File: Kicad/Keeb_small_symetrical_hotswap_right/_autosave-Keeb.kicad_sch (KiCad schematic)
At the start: 32 parts, among them J2 B2B-XH-A_LF__SN_, J3 MJ-4PP-9_MJ-4PP-9, SW1 CherryMX, SW10 CherryMX, SW11 CherryMX, SW13 CherryMX, SW14 CherryMX, SW15 CherryMX, SW16 CherryMX, SW17 CherryMX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

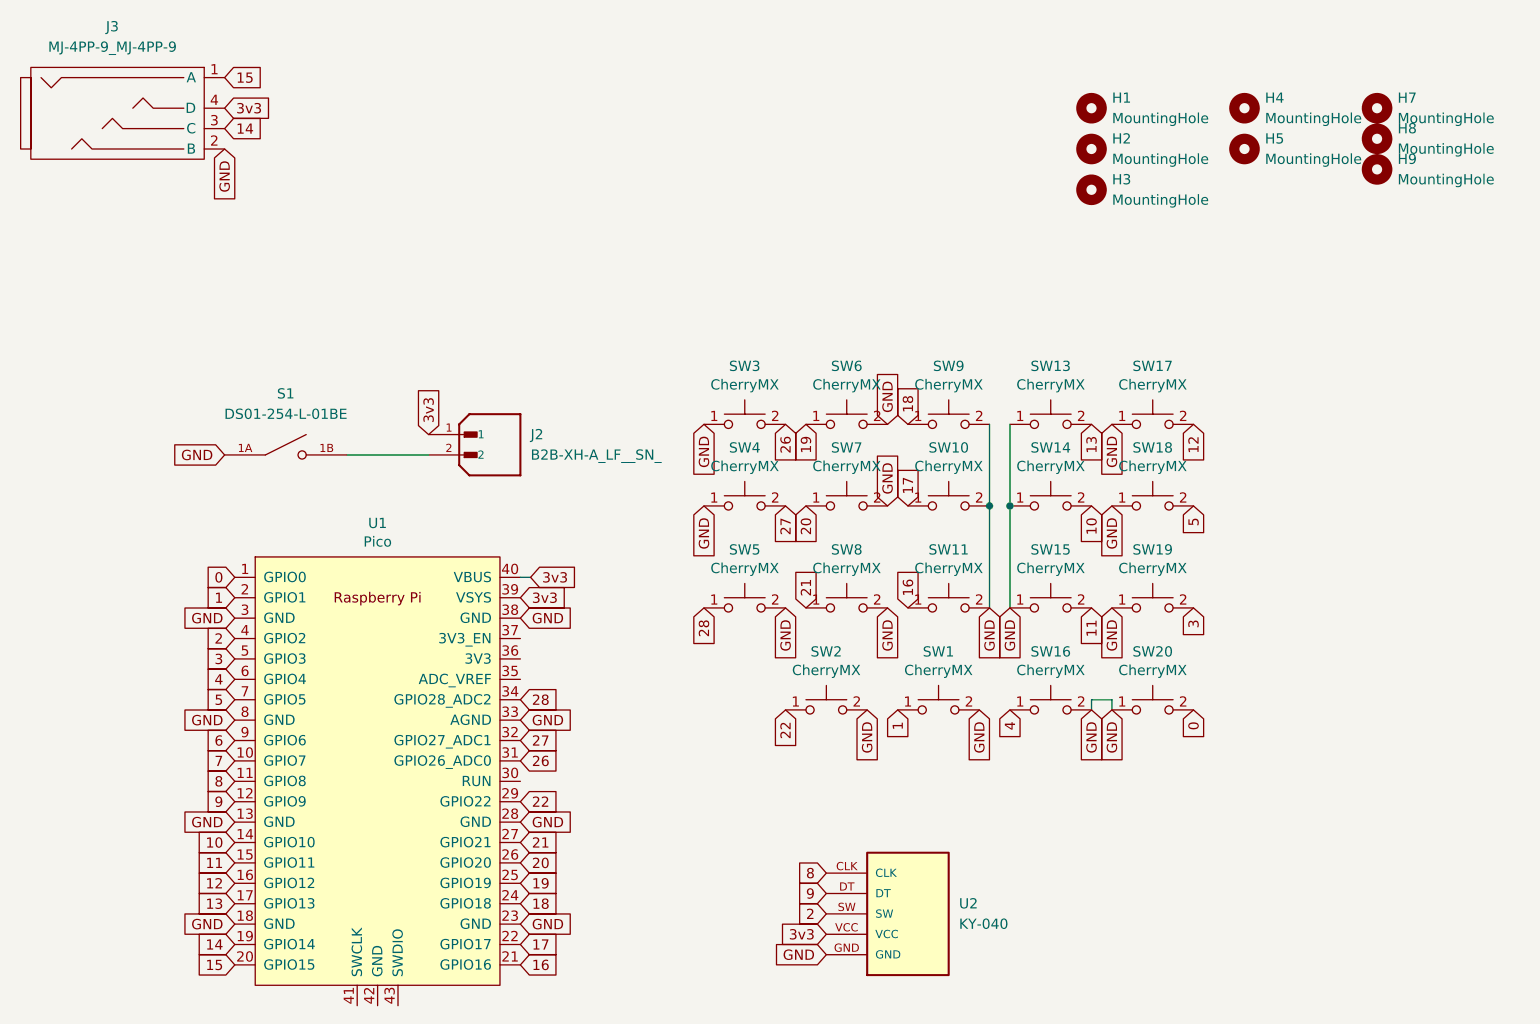
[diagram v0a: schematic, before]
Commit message: Implemented encoders on the split halves
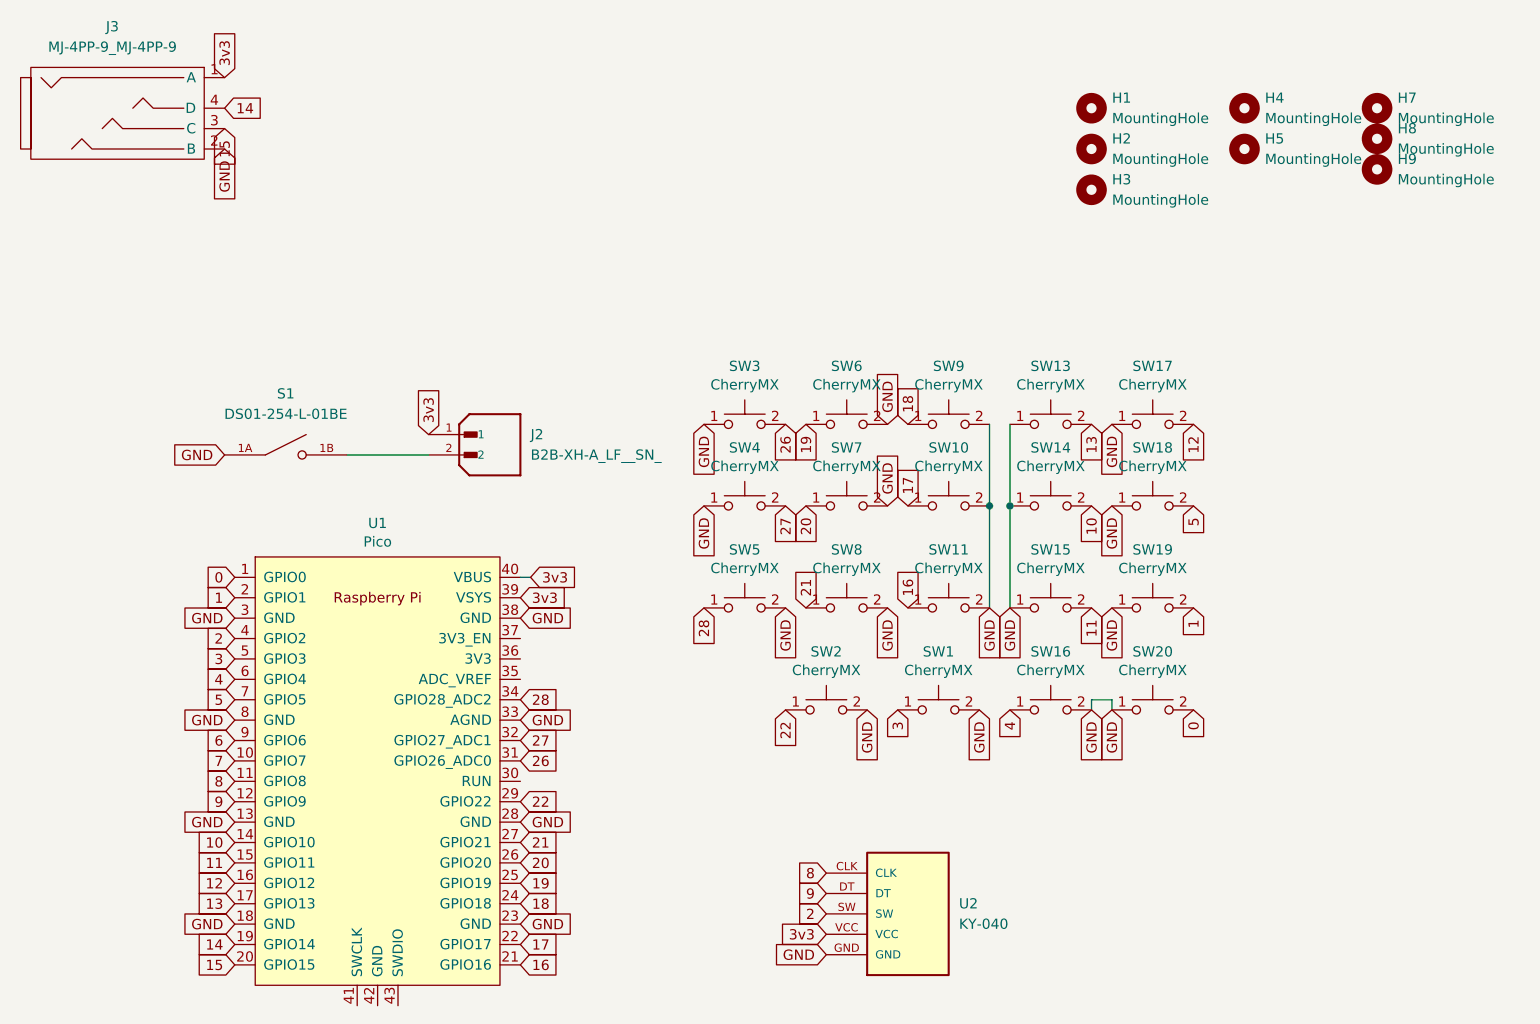
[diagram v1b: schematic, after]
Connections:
- net 1: now also SW19.2; no longer SW1.1
- net 14: now also J3.4 (D); no longer J3.3 (C)
- net 15: now also J3.3 (C); no longer J3.1 (A)
- net 3: now also SW1.1; no longer SW19.2
- net 3v3: now also J3.1 (A); no longer J3.4 (D)
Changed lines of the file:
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@@
     )
   )
-  (global_label "1" (shape input) (at 132.08 97.79 270) (fields_autoplaced)
+  (global_label "3" (shape input) (at 132.08 97.79 270) (fields_autoplaced)
     (effects (font (size 1.27 1.27)) (justify right))
     (property "Intersheetrefs" "${INTERSHEET_REFS}" (at 132.08 101.3305 90)
@@
     )
   )
-  (global_label "14" (shape input) (at 48.26 25.4 0) (fields_autoplaced)
-    (effects (font (size 1.27 1.27)) (justify left))
-    (property "Intersheetrefs" "${INTERSHEET_REFS}" (at 53.01 25.4 0)
-      (effects (font (size 1.27 1.27)) (justify left) hide)
-    )
-  )
   (global_label "28" (shape input) (at 107.95 85.09 270) (fields_autoplaced)
     (effects (font (size 1.27 1.27)) (justify right))
@@
     )
   )
-  (global_label "15" (shape input) (at 48.26 19.05 0) (fields_autoplaced)
-    (effects (font (size 1.27 1.27)) (justify left))
-    (property "Intersheetrefs" "${INTERSHEET_REFS}" (at 53.01 19.05 0)
+  (global_label "14" (shape input) (at 48.26 22.86 0) (fields_autoplaced)
+    (effects (font (size 1.27 1.27)) (justify left))
+    (property "Intersheetrefs" "${INTERSHEET_REFS}" (at 53.01 22.86 0)
       (effects (font (size 1.27 1.27)) (justify left) hide)
     )
@@
     )
   )
+  (global_label "15" (shape input) (at 48.26 25.4 270) (fields_autoplaced)
+    (effects (font (size 1.27 1.27)) (justify right))
+    (property "Intersheetrefs" "${INTERSHEET_REFS}" (at 48.26 30.15 90)
+      (effects (font (size 1.27 1.27)) (justify right) hide)
+    )
+  )
   (global_label "GND" (shape input) (at 118.11 85.09 270) (fields_autoplaced)
     (effects (font (size 1.27 1.27)) (justify right))
@@
     )
   )
-  (global_label "3" (shape input) (at 168.91 85.09 270) (fields_autoplaced)
+  (global_label "1" (shape input) (at 168.91 85.09 270) (fields_autoplaced)
     (effects (font (size 1.27 1.27)) (justify right))
     (property "Intersheetrefs" "${INTERSHEET_REFS}" (at 168.91 88.6305 90)
@@
     )
   )
-  (global_label "3v3" (shape input) (at 48.26 22.86 0) (fields_autoplaced)
-    (effects (font (size 1.27 1.27)) (justify left))
-    (property "Intersheetrefs" "${INTERSHEET_REFS}" (at 53.9776 22.86 0)
-      (effects (font (size 1.27 1.27)) (justify left) hide)
-    )
-  )
   (global_label "26" (shape input) (at 118.11 62.23 270) (fields_autoplaced)
     (effects (font (size 1.27 1.27)) (justify right))
@@
       (effects (font (size 1.27 1.27)) (justify left) hide)
     )
+  )
+  (global_label "3v3" (shape input) (at 48.26 19.05 90) (fields_autoplaced)
+    (effects (font (size 1.27 1.27)) (justify left))
+    (property "Intersheetrefs" "${INTERSHEET_REFS}" (at 48.26 13.3324 90)
+      (effects (font (size 1.27 1.27)) (justify left) hide)
+    )
